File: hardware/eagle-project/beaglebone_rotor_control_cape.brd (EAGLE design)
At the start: 71.8 x 54.6 mm, 29 parts, among them IC1 TLC2264CDU, IC2 MCP4901, IC3 MAX3232ESE, Q1 SQ2348ES-T1-GE3, Q2 SQ2348ES-T1-GE3, X1 BEAGLEBONE_OUTLINE

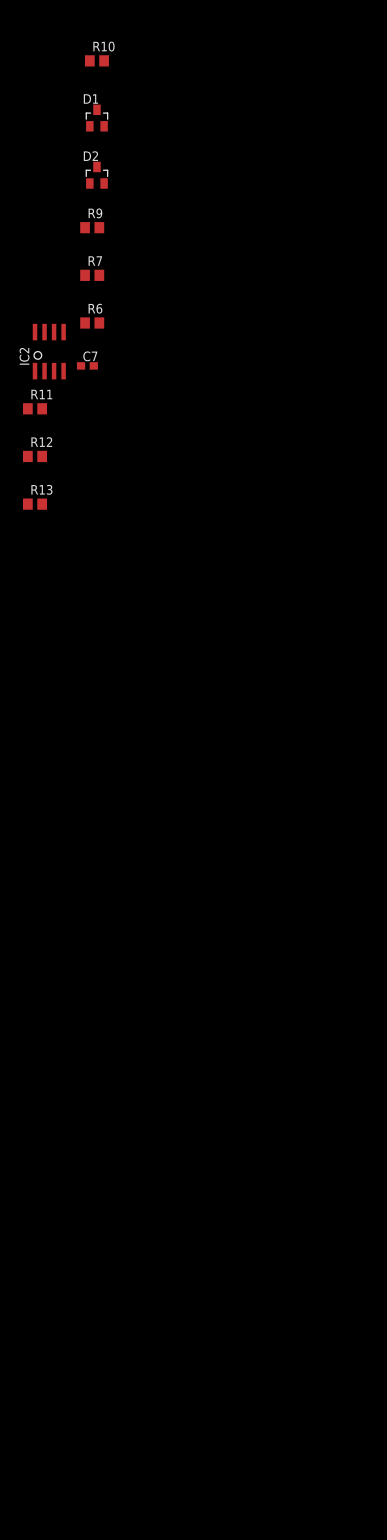
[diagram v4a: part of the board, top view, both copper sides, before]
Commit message: Hardware: Create ERC5-AP interface
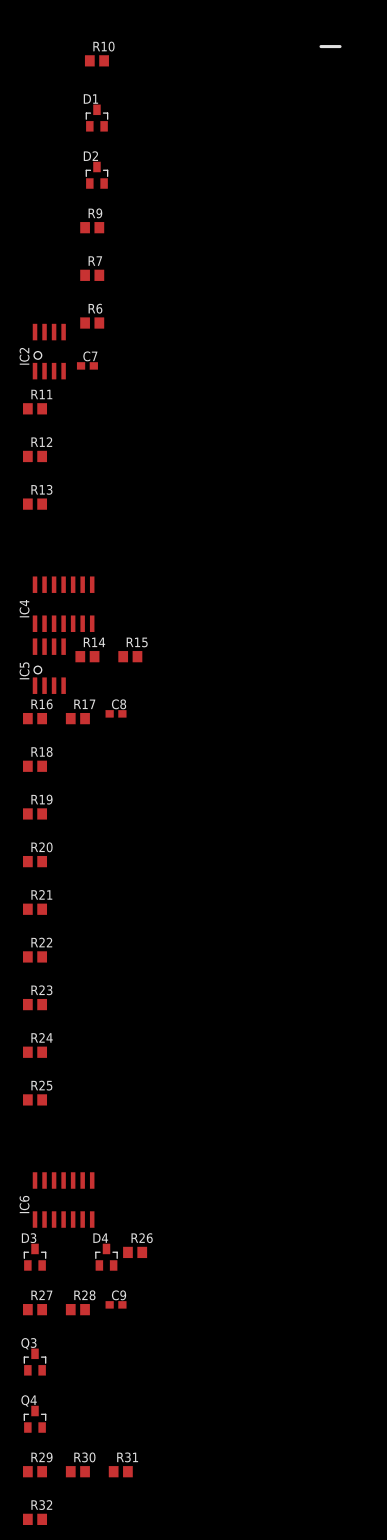
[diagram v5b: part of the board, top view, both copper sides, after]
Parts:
- added C8, C9: 100n, rcl:C0603
- added D3: BAS40-04, diode:SOT23
- added D4: 5V1, diode:SOT23
- added IC4, IC6: TLC2264CDU, ti-tlc2264cd:SO14
- added IC5: MCP4901, microchip_mcp4901:SO-08
- added Q3, Q4: SQ2348ES-T1-GE3, vishay_sq2348eS-t1-ge3:SOT23
- added R14, R18, R19, R20, R21, R22, R23, R24, R25, R31, R32: 100, rcl:R0805
- added R15: 0, rcl:R0805
- added R16: 5k, rcl:R0805
- added R17, R26, R28: 10k, rcl:R0805
- added R27: 5k6, rcl:R0805
- added R29, R30: 1M, rcl:R0805
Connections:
- new net BB_AIN2: C9.1, R26.1, R27.2
- new net N$10: IC2.3, R19.2
- new net N$23: R25.1
- new net N$24: R24.1
- new net N$26: R23.1
- new net N$27: IC5.4, R23.2
- new net N$28: IC5.3, R24.2
- new net N$29: IC5.2, R25.2
- new net N$30: R22.1
- new net N$31: IC4.3, IC5.8
- new net N$32: IC4.1, R14.1, R16.2
- new net N$33: IC4.2, R16.1, R17.2
- new net N$34: R31.1
- new net N$35: IC6.6, IC6.7, R26.2
- new net N$36: D3.3, D4.3, IC6.5, R28.1
- new net N$37: R32.1
- new net N$38: Q3.1, R29.2, R32.2
- new net N$39: Q4.1, R30.2, R31.2
- new net N$4: IC5.5, R15.2, R22.2
- new net N$6: IC2.2, R18.2
- new net N$8: R21.1
- new net N$9: IC2.4, R20.2
- new net ROT_E_DOWN: Q4.3
- new net ROT_E_POSITION: R28.2
- new net ROT_E_SPEED: R14.2
- new net ROT_E_UP: Q3.3
- new net V+: IC6.4
- new net V-: IC6.11
- net +3V3: now also C7.1, C8.1, IC2.1, IC2.6, IC5.1, IC5.6
- net +5V: now also D3.2, IC4.4; no longer C7.1, IC2.1, IC2.6
- net BB_SPI0_CS0: now also R18.1; no longer IC2.2
- net BB_SPI0_D0: now also R20.1; no longer IC2.4
- net BB_SPI0_SCLK: now also R19.1; no longer IC2.3
- net GND: now also C8.2, C9.2, D3.1, D4.1, IC4.11, IC5.7, Q3.2, Q4.2, R15.1, R17.1, R27.1, R29.1, R30.1
- net N$7: now also R21.2
